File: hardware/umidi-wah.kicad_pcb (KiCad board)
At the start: 2 copper layers, 129 x 107 mm, 87 parts, among them J1 Power, J2 Pots Main, J3 Pots Front, J4 Switch, J5 Input, J6 Output, J7 Conn_02x05_Odd_Even, J8 Conn_02x05_Odd_Even, K1 G6K-2P-Y-DC5, Q1 KSC1815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

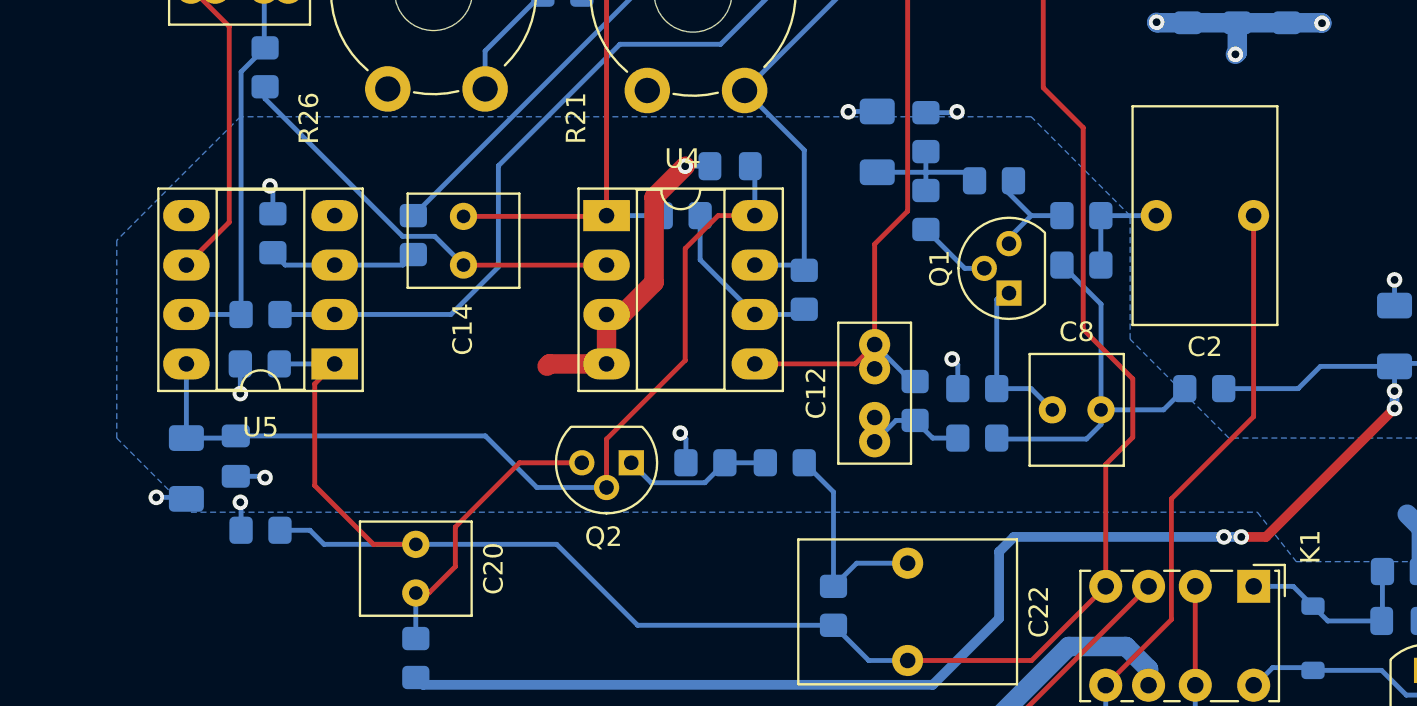
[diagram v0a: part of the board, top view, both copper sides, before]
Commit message: Make C8 footprint more generic (2.5 or 5mm pin distance)
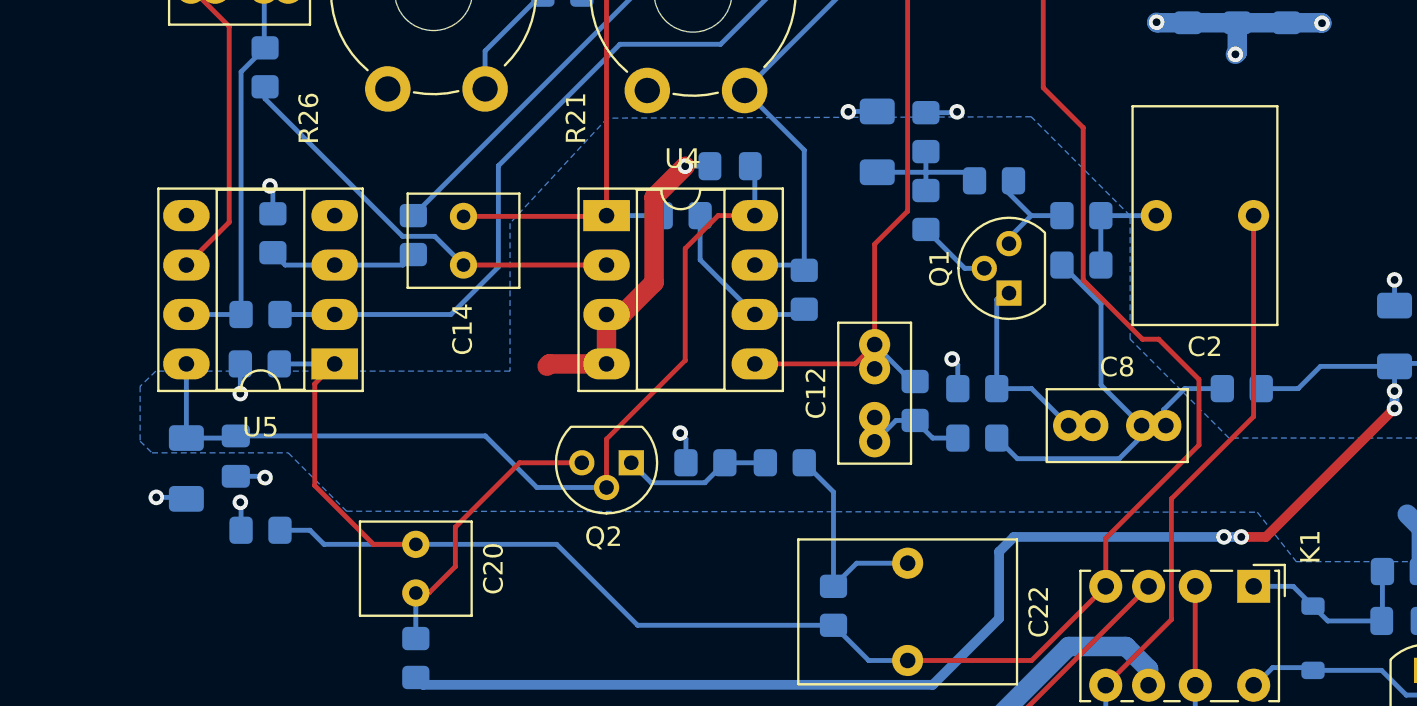
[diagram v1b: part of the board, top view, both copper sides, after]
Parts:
- C8: footprint Capacitor_THT:C_Rect_L4.6mm_W5.5mm_P2.50mm_MKS02_FKP02 -> Capacitor_THT:C_Rect_L7.0mm_W3.5mm_P2.50mm_P5.00mm
- moved R7 1.93 mm to (130.2, 88.9)
- moved C8 1.16 mm to (121.3, 90.8)
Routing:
- net Net-(C8-Pad2): track 19.5 -> 23.6 mm
- net /wah_out: track 153.8 -> 157.1 mm
- net vmid: track 74.8 -> 72.8 mm
- net Net-(Q1-E): track 8.60 -> 9.77 mm

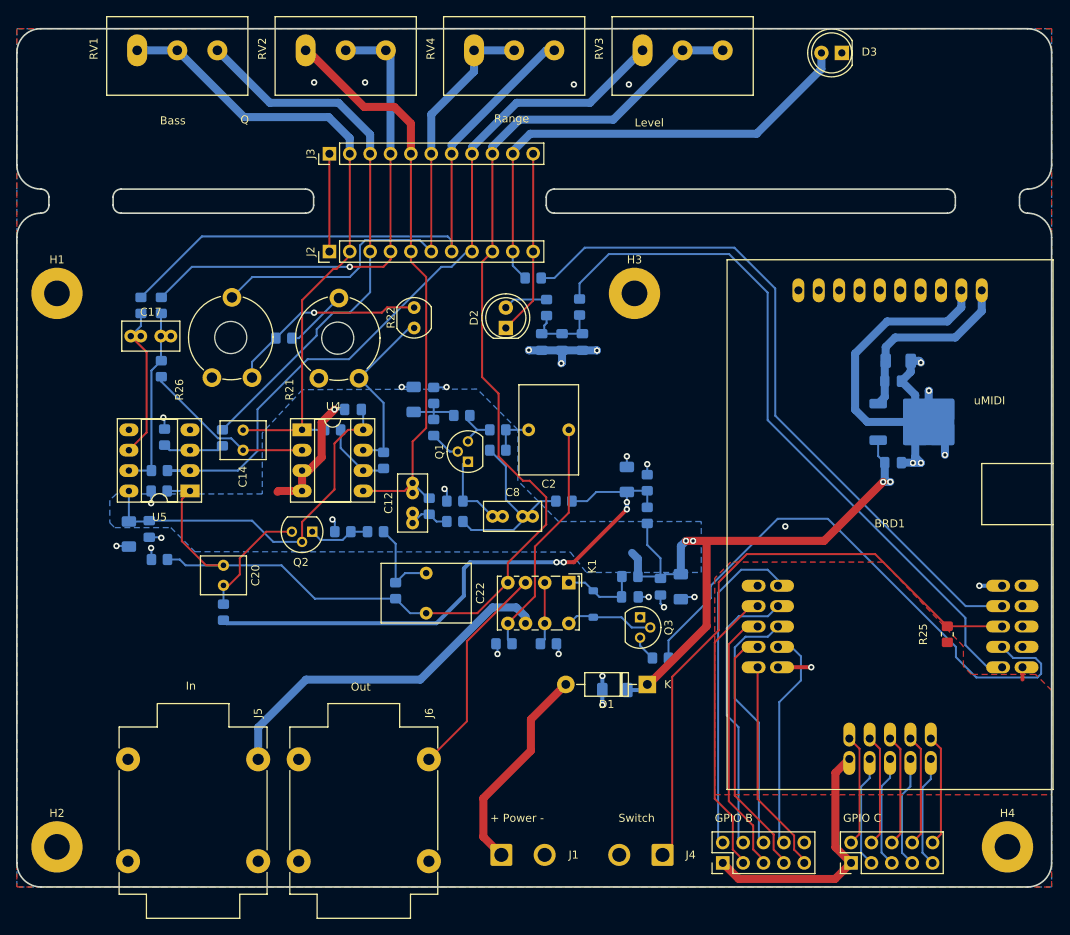
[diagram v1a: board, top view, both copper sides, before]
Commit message: Redesign 9V distribution
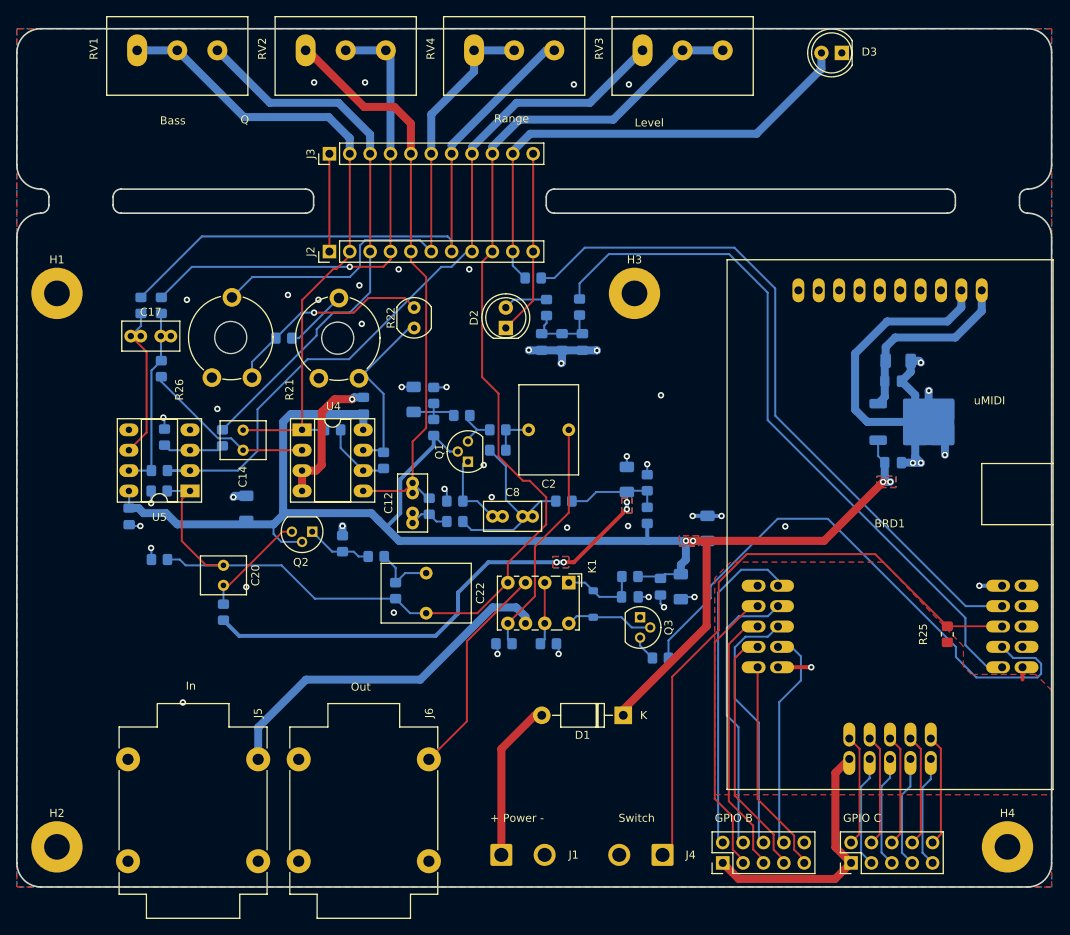
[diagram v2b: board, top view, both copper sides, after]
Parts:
- moved C4 23.2 mm to (148.1, 92.3), turned to 90 degrees
- moved C7 15.0 mm to (90.6, 89.8), turned to 90 degrees
- moved D1 4.88 mm to (137.6, 115.6)
- moved R36 3.09 mm to (106.8, 95.8)
- moved C1 2.96 mm to (76.0, 90.8)
- moved R34 1.49 mm to (102.6, 94.2), turned to -90 degrees
- moved C3 1.38 mm to (105.2, 77.0), turned to 90 degrees
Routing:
- net +9V: track 130.5 -> 197.9 mm
- net Net-(D1-A): track 26.4 -> 20.0 mm
- net Net-(C22-Pad1): track 11.3 -> 8.15 mm
- net Net-(Q2-B): track 14.8 -> 13.6 mm
- net Net-(R22-Pad2): track 25.0 -> 26.0 mm
- net vmid: track 72.8 -> 73.7 mm
- net GND: track 169.2 -> 170.0 mm, vias 34 -> 50
- net Net-(R15-Pad2): track 22.6 -> 23.3 mm
- net Net-(Q2-E): track 7.74 -> 8.25 mm
- added copper zone on F.Cu, net +9V
- added copper zone on B.Cu, net vmid
- added copper zone on F.Cu, net vmid

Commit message: Increase trace widths (and more brd optimization)
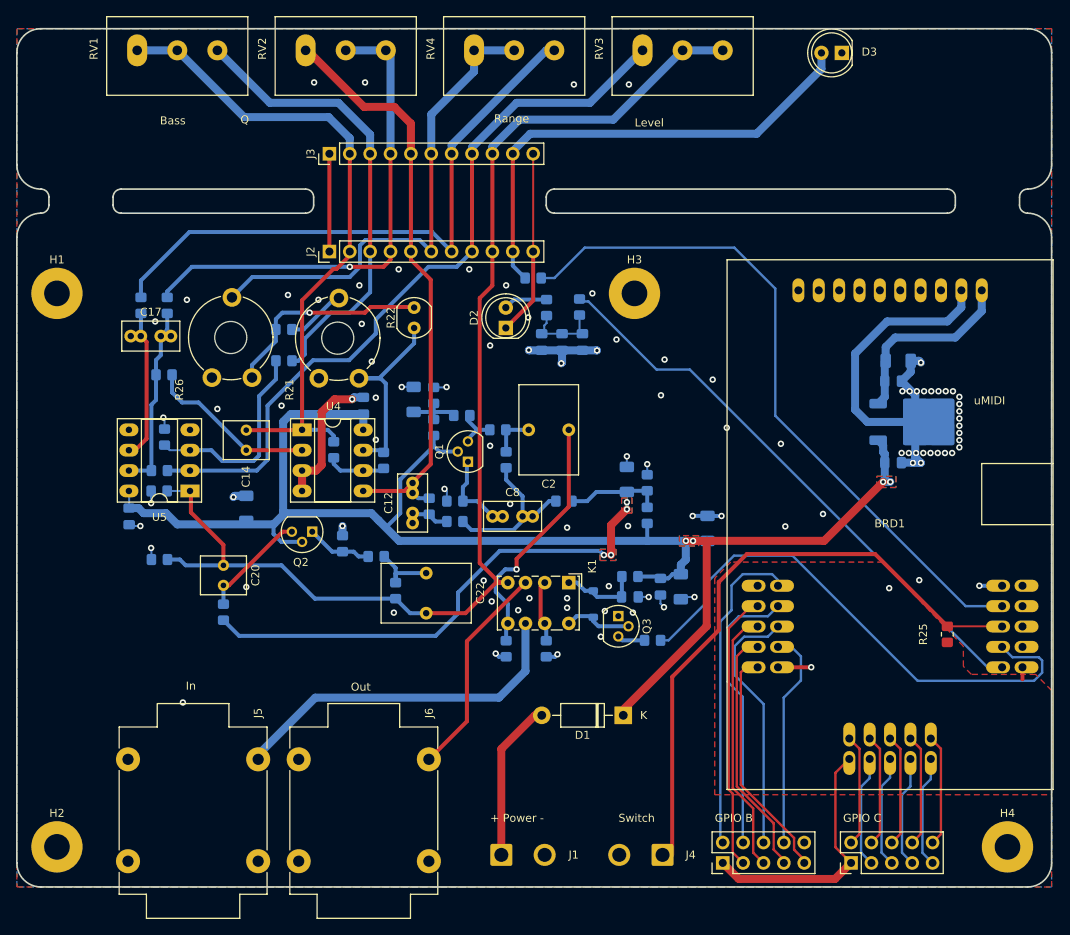
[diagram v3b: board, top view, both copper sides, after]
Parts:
- moved R17 12.3 mm to (95.3, 71.4), turned to 180 degrees
- moved Q3 2.72 mm to (137.0, 103.2)
- moved R13 2.49 mm to (101.5, 82.5), turned to -90 degrees
- moved R35 2.42 mm to (141.2, 106.2)
- moved R5 1.59 mm to (123.0, 83.8), turned to 90 degrees
- moved R23 1.08 mm to (95.3, 67.5)
- moved R14 0.83 mm to (80.3, 73.2), turned to 180 degrees
- moved R16 0.74 mm to (80.8, 64.5)
- moved R32 0.68 mm to (128.0, 107.3), turned to 90 degrees
- moved R31 0.68 mm to (123.0, 107.3), turned to 90 degrees
- moved C14 0.39 mm to (90.6, 82.5)
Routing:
- net Net-(U5A-+): track 7.70 -> 25.6 mm
- net /led_pwm: track 88.8 -> 71.7 mm
- net /Filter/rv1_2: track 70.1 -> 58.1 mm
- net GND: track 170.0 -> 164.3 mm, vias 50 -> 99
- net /wah_out: track 157.1 -> 151.4 mm
- net /bypass_n: track 72.6 -> 67.4 mm
- net Net-(C8-Pad2): track 23.6 -> 20.4 mm
- net vmid: track 73.7 -> 76.3 mm
- net Net-(BRD1B-PA7(ADC7)): track 26.8 -> 29.4 mm
- net Net-(D4-A): track 11.4 -> 8.91 mm
- net Net-(R15-Pad2): track 23.3 -> 25.6 mm
- net /Filter/rv1_1: track 80.3 -> 82.5 mm
- net Net-(U5B--): track 19.3 -> 21.2 mm
- net /Filter/rv3_1: track 94.8 -> 96.4 mm
- net /wah_in: track 30.0 -> 31.6 mm, vias 0 -> 1
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
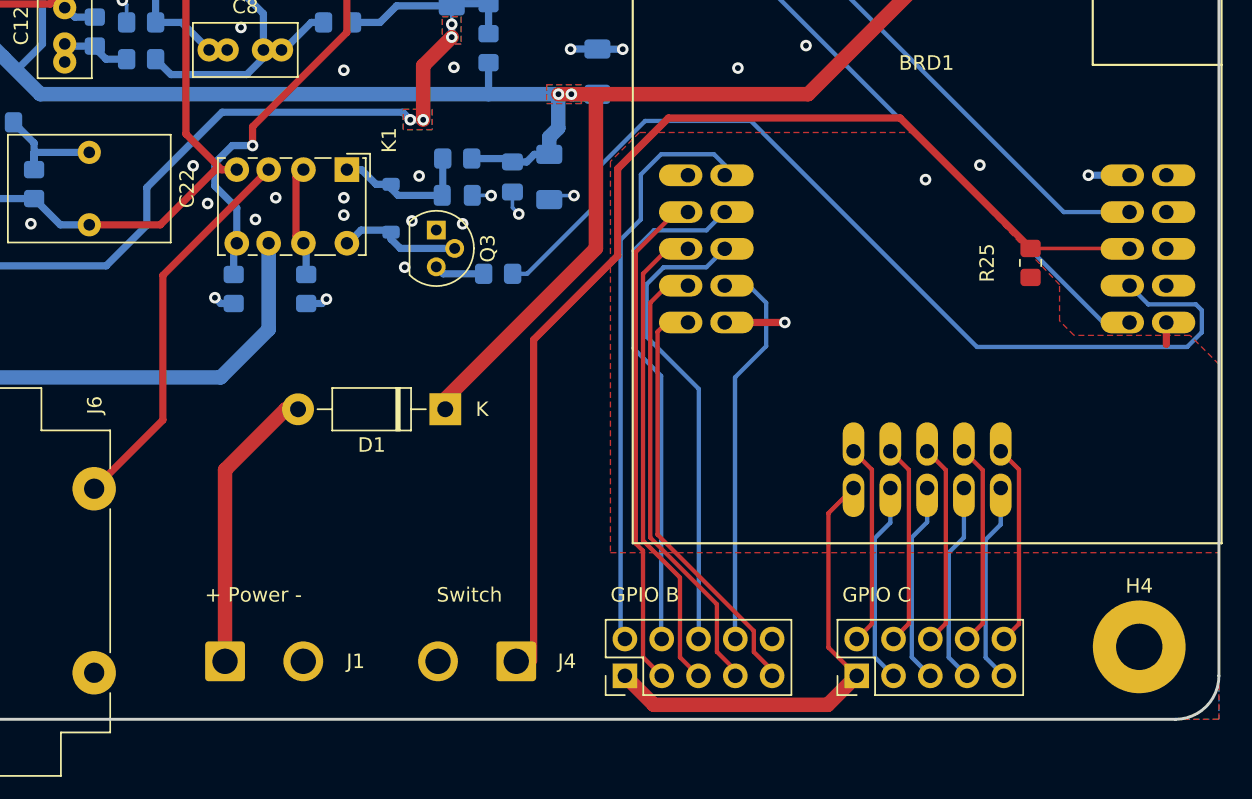
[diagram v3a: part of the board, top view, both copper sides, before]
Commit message: Optimize routing of umidi-3,3v
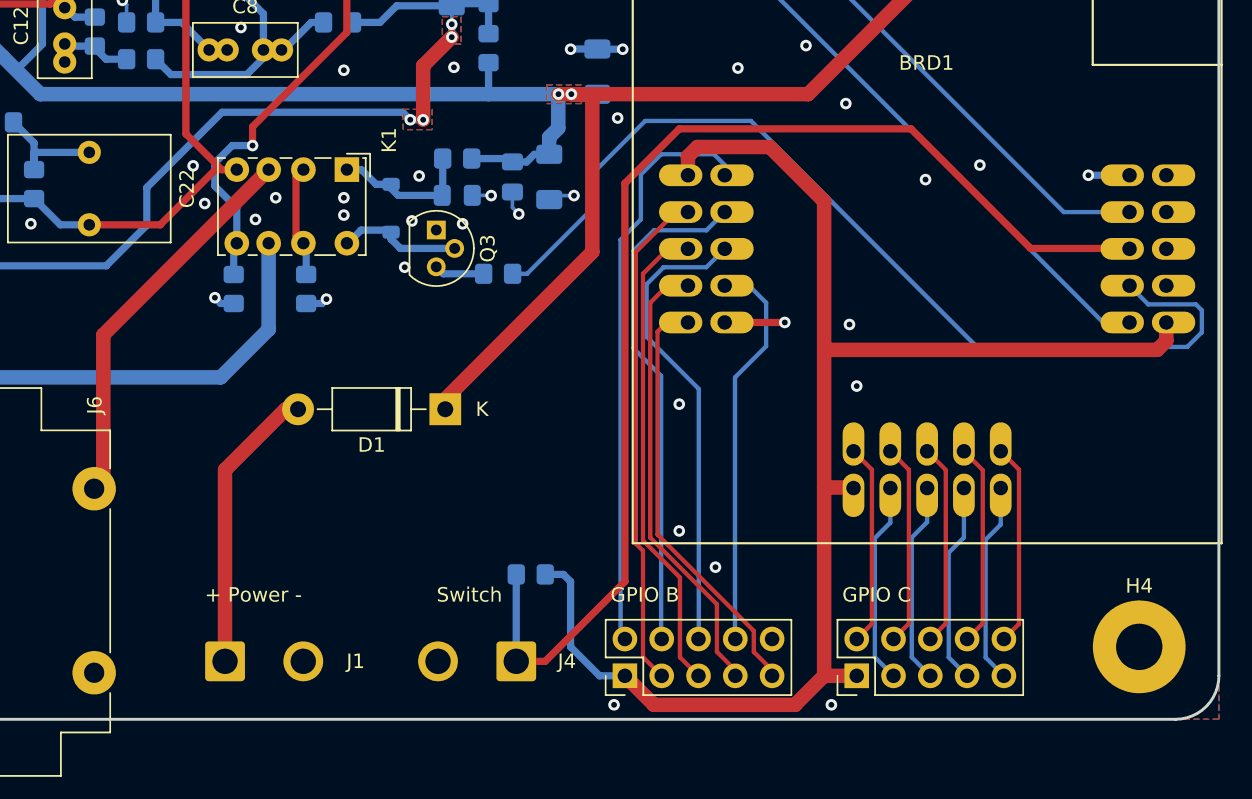
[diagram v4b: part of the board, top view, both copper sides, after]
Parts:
- R25: moved to B.Cu
- moved R25 40.7 mm to (143.5, 127.0), turned to 0 degrees
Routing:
- net /umidi_3v3: track 33.7 -> 101.3 mm
- net /toggle_switch: track 76.9 -> 81.9 mm
- net GND: vias 99 -> 108
- removed copper zone on F.Cu, net /umidi_3v3

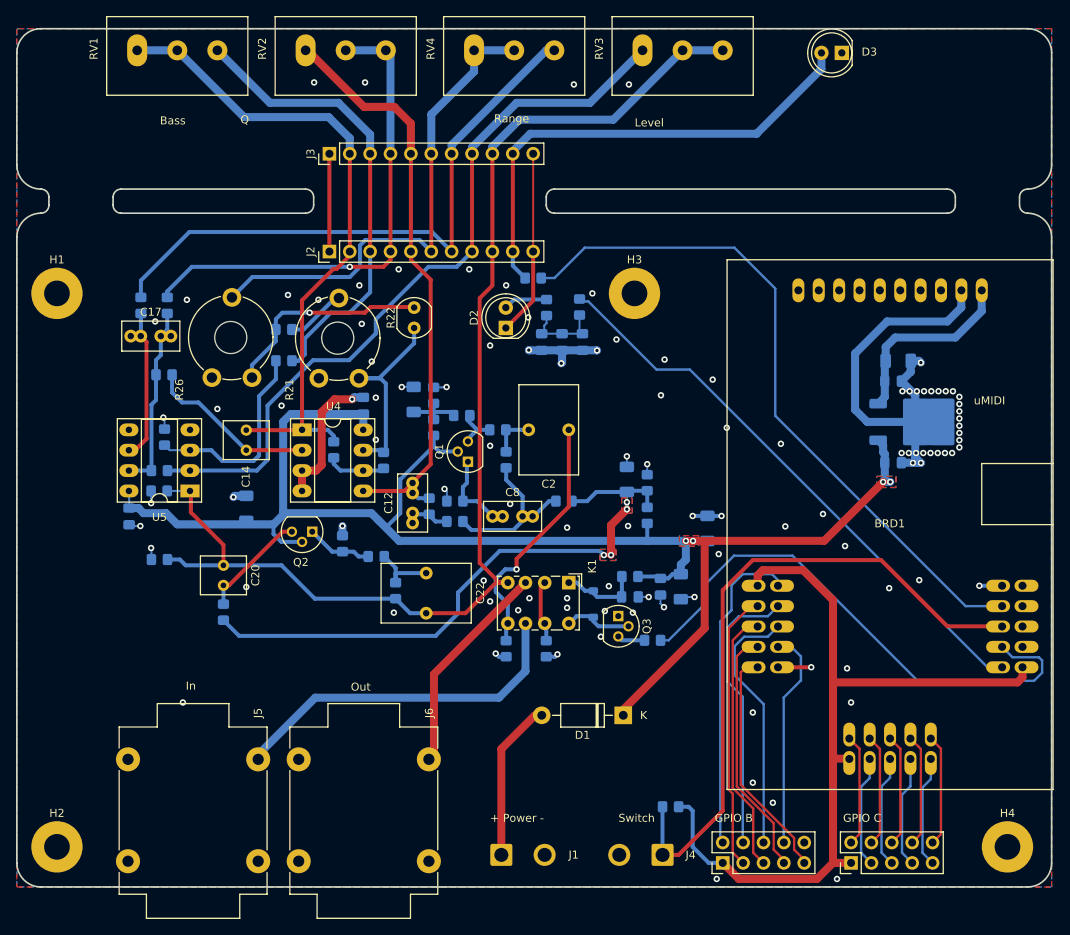
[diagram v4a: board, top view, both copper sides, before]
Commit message: Add artwork to solder mask and copper
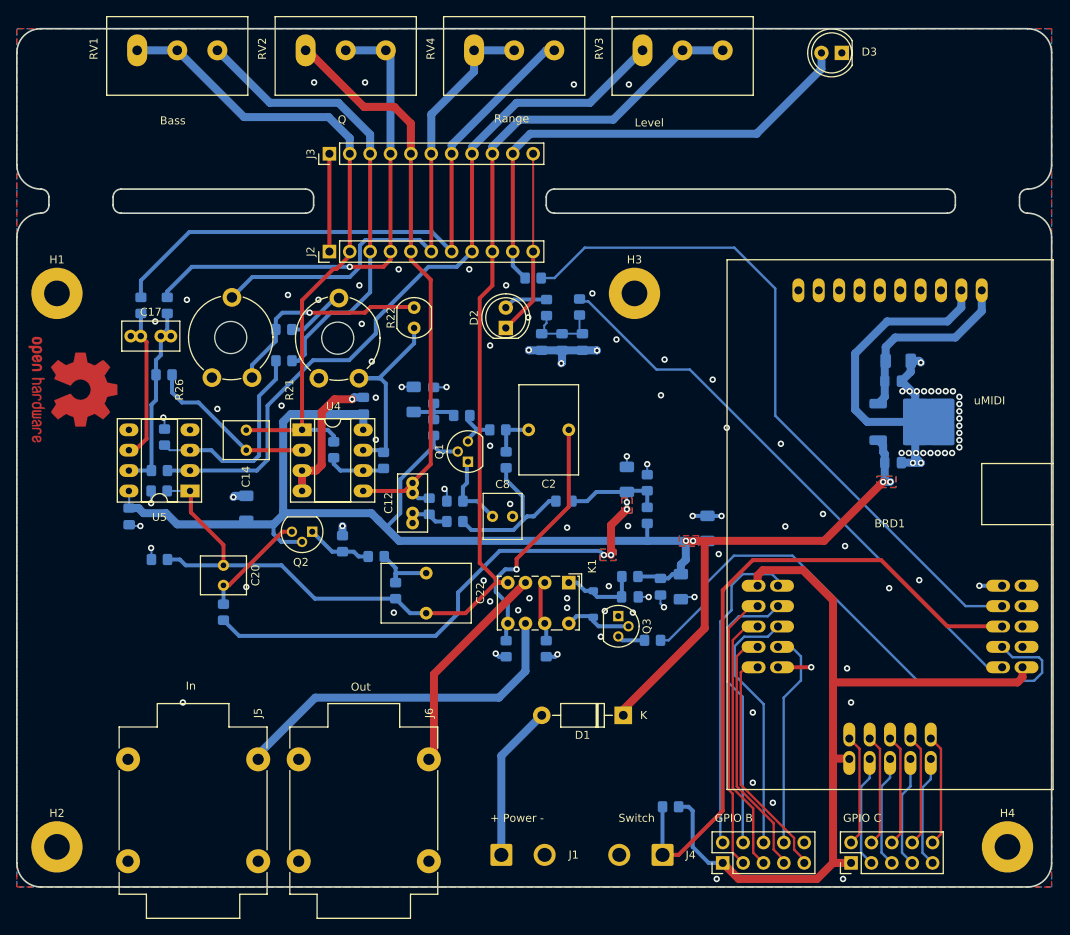
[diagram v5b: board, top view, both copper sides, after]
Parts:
- added REF**: OSHW-Logo2_14.6x12mm_Copper, Symbol:OSHW-Logo2_14.6x12mm_Copper, F.Cu at (69.0, 75.0)
- C8: footprint Capacitor_THT:C_Rect_L7.0mm_W3.5mm_P2.50mm_P5.00mm -> Capacitor_THT:C_Rect_L4.6mm_W5.5mm_P2.50mm_MKS02_FKP02
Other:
- board text added: "+ pwr -"
- board text added: "in"
- board text added: "out"
- board text added: "sw"
- board text added: "umidi-wah 0.5 {dblquote}daemon{dblquote} [2024]"
